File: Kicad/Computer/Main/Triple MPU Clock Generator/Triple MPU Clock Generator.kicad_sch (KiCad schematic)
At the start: 48 parts, among them CN1 CA0612KRX7R9BB100, CN2 CA0612KRX7R9BB100, CN3 CA0612KRX7R9BB100, CN4 CA0612KRX7R9BB100, CN5 CA0612KRX7R9BB100, CN7 CA0612KRX7R9BB100, CN8 CA0612KRX7R9BB100, IC1 AP7365-33WG-7, IC10 74LVC74APW,118, IC11 74LVC157APW,118, IC12 74LVC1G08GV,125, IC13 74LVC14APW,118, IC2 74LVC74APW,118, IC3 74LVC74APW,118, IC4 74LVC74APW,118, IC5 74LVC74APW,118, IC6 74LVC74APW,118, IC7 74LVC157APW,118, IC8 DS1813R-10+T&R, J10 Pin_Header_01x32, J11 Pin_Header_01x32, J2 Conn_02x32_Counter_Clockwise, J4 Conn_01x04_Socket, J5 Conn_01x04_Socket

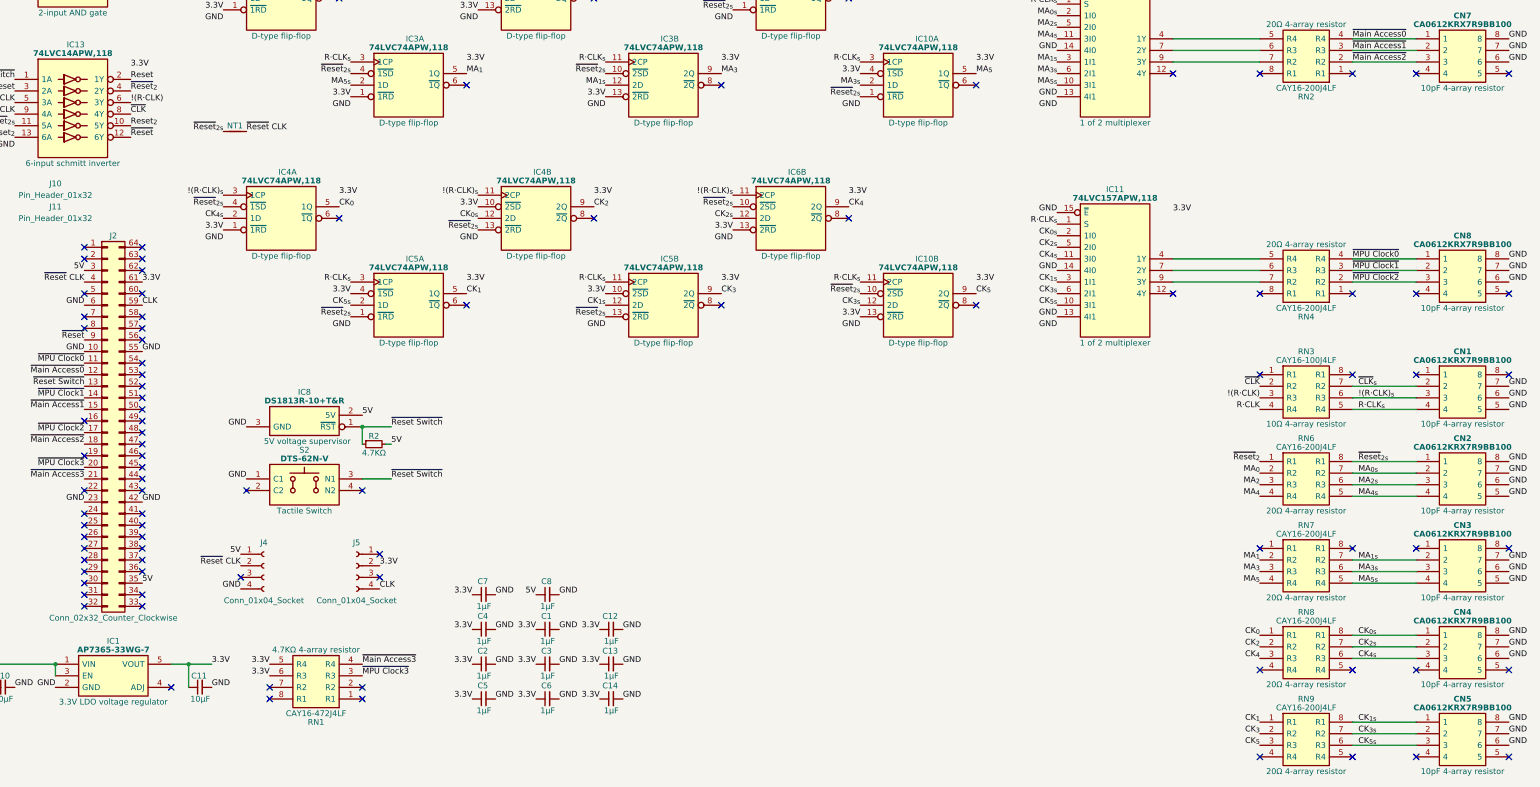
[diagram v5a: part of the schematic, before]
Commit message: Added a (potentially) 50MHz board.
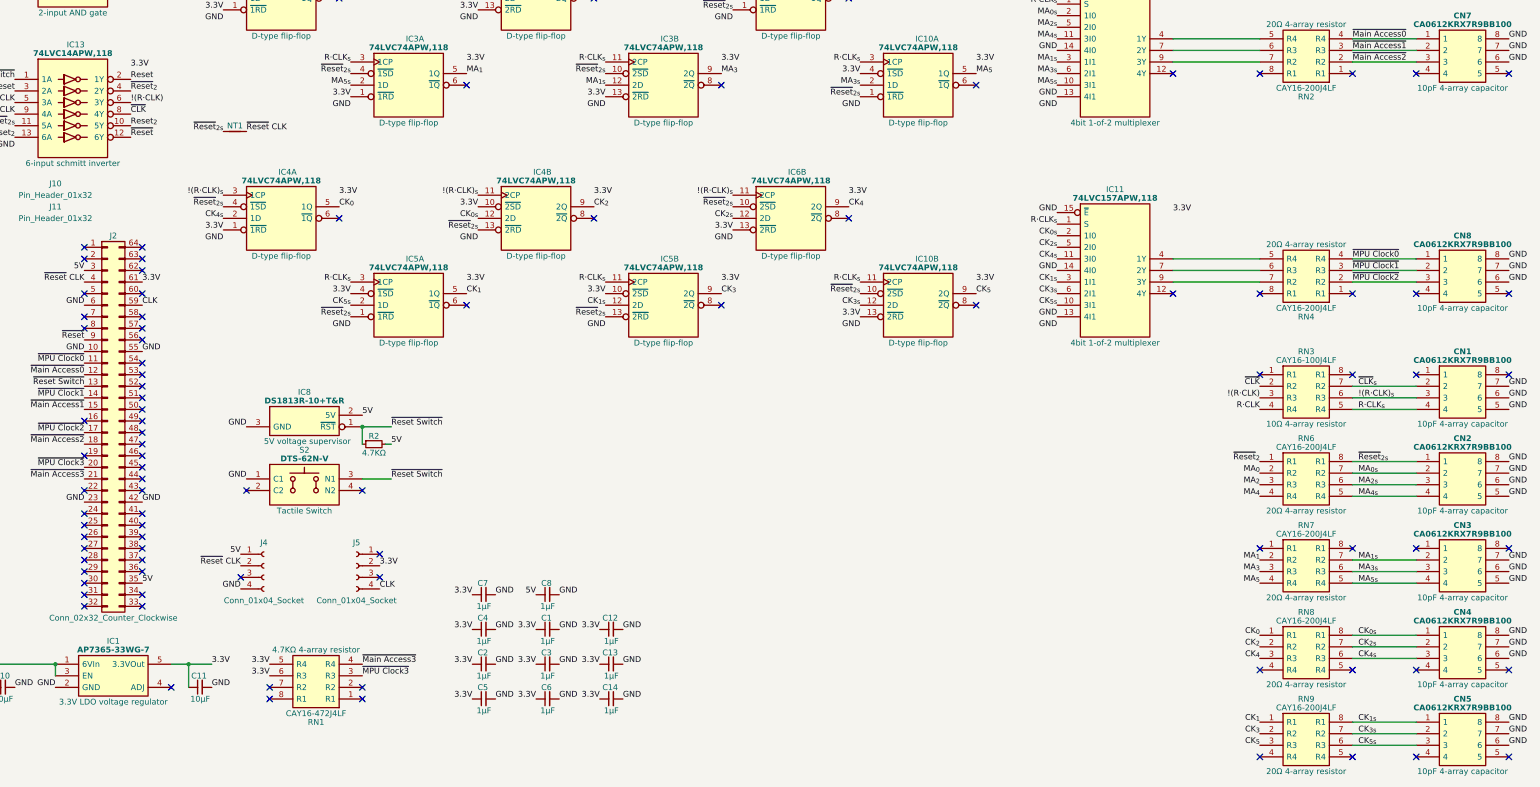
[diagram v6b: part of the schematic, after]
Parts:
- IC1: footprint SOT95P285X130-5N -> SamacSys_Parts:SOT95P285X130-5N; Garbage (none) -> DiodesZetex AP7365-33WG-7, LDO Voltage Regulator, 600mA, 3.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
- IC10, IC2, IC3, IC4, IC5, IC6: footprint SOP65P640X110-14N -> SamacSys_Parts:SOP65P640X110-14N; Garbage (none) -> 74LVC74A - Dual D-type flip-flop with set and reset; positi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
- IC11, IC7: footprint SOP65P640X110-16N -> SamacSys_Parts:SOP65P640X110-16N; Garbage (none) -> NEXPERIA - 74LVC157APW,118 - MUX, QUAD, 8 I/P, TSSOP-16
- IC12: footprint SOT95P275X110-5N -> SamacSys_Parts:SOT95P275X110-5N; Garbage (none) -> NEXPERIA - 74LVC1G08GV,125 - LOGIC, AND GATE, DUAL I/P, SC-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
- IC13: footprint SOP65P640X110-14N -> SamacSys_Parts:SOP65P640X110-14N; Garbage (none) -> 74LVC14A - Hex inverting Schmitt trigger with 5 V tolerant 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
- IC8: footprint SOT95P237X112-3N -> SamacSys_Parts:SOT95P237X112-3N; Garbage (none) -> Maxim DS1813R-10+T&R, Voltage Supervisor 4.25 4.49 V, Reset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
- J4, J5: footprint Connector_PinSocket_2.54mm:PinSocket_1x04_P2.54mm_Vertical -> (none)
- NT1: footprint NetTie:NetTie-2_SMD_Pad0.5mm -> SamacSys_Parts:NetTie:NetTie-2_SMD_Pad0.5mm
- RN1: Garbage (none) -> Bourns CAY16 Series 4.7k +/-5% Isolated SMT Resistor Array,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
- RN2, RN4, RN6, RN7, RN8, RN9: Arrow Part Number CAY16-331J4LF -> (none); Arrow Price/Stock https://www.arrow.com/en/products/cay16-331j4lf/bourns?regi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 -> (none)
- RN3: Garbage (none) -> Bourns CAY16 Series 10 +/-5% Isolated SMT Resistor Array, 4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
- S2: footprint DTS62NV -> SamacSys_Parts:DTS62NV; Garbage (none) -> Tactile Switches Through Hole 6*6

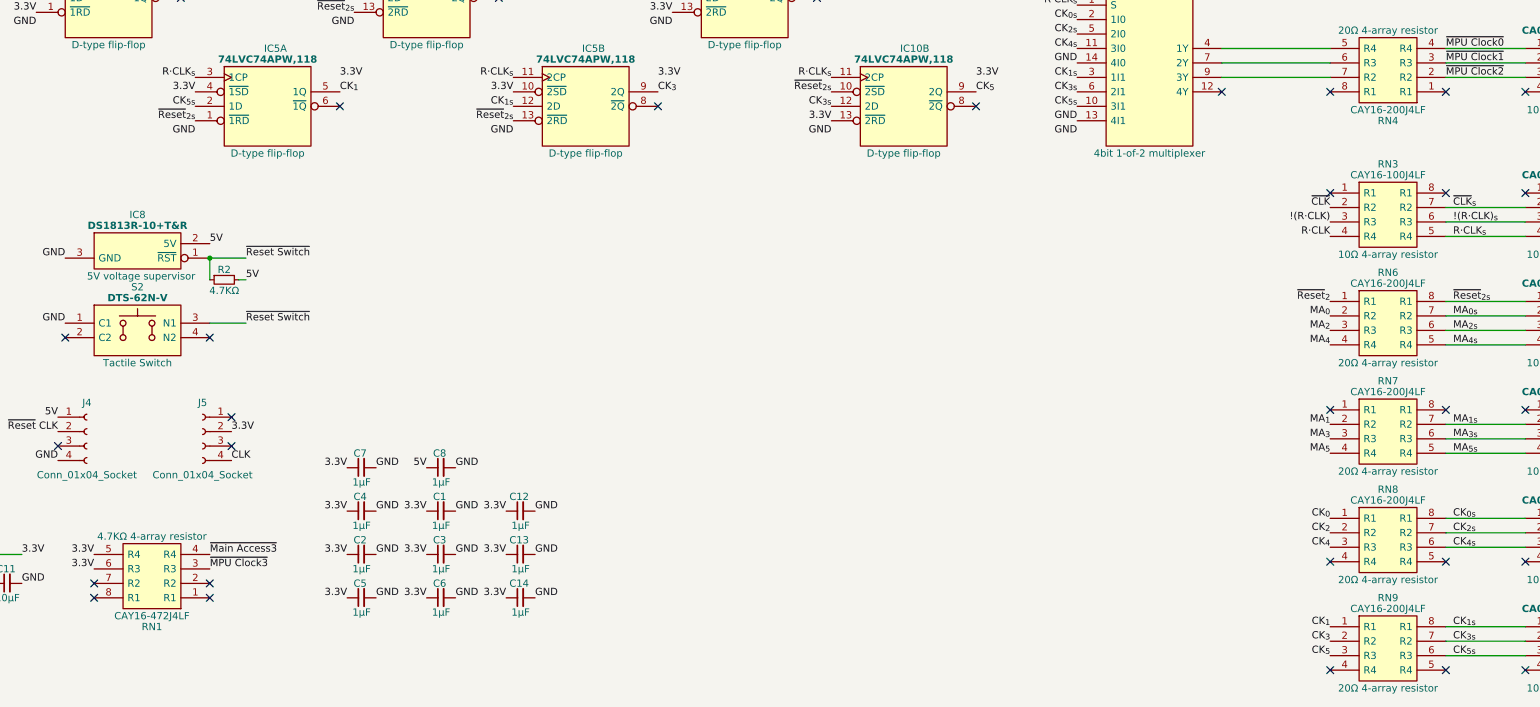
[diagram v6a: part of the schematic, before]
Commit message: Generated Gerbers for clock generators.
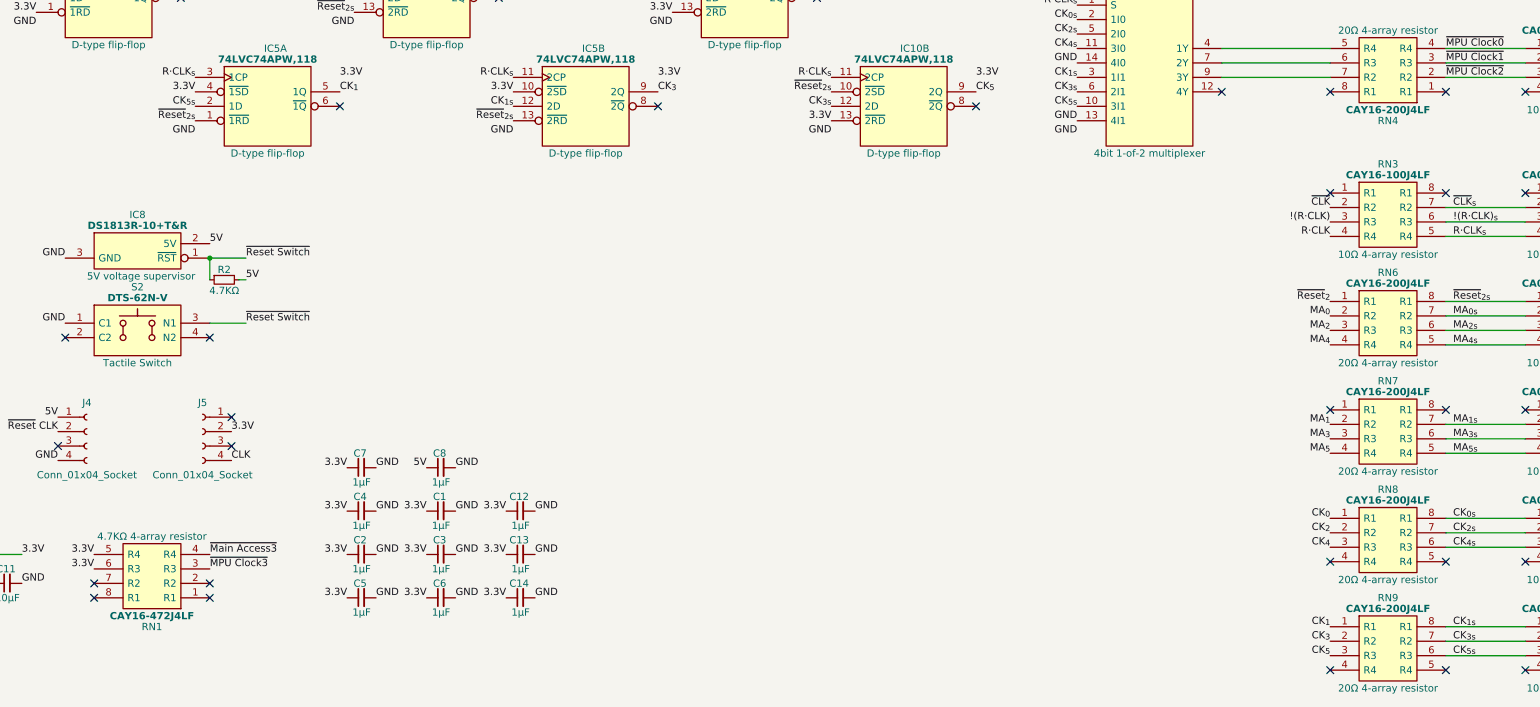
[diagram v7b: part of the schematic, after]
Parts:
- IC1: Garbage DiodesZetex AP7365-33WG-7, LDO Voltage Regulator, 600mA, 3.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 -> (none)
- IC8: Garbage Maxim DS1813R-10+T&R, Voltage Supervisor 4.25 4.49 V, Reset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 -> (none)
- J4, J5: footprint (none) -> Connector_PinSocket_2.54mm:PinSocket_1x04_P2.54mm_Vertical
- NT1: footprint SamacSys_Parts:NetTie:NetTie-2_SMD_Pad0.5mm -> NetTie:NetTie-2_SMD_Pad0.5mm
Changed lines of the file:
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@@
 			)
 		)
-		(property "Footprint" ""
+		(property "Footprint" "Connector_PinSocket_2.54mm:PinSocket_1x04_P2.54mm_Vertical"
 			(at 95.25 189.23 0)
 			(effects
@@
 				(font
 					(size 1.27 1.27)
+					(bold yes)
 				)
 			)
@@
 			)
 		)
-		(property "Footprint" "SamacSys_Parts:NetTie:NetTie-2_SMD_Pad0.5mm"
+		(property "Footprint" "NetTie:NetTie-2_SMD_Pad0.5mm"
 			(at 107.315 100.965 0)
 			(effects
@@
 				(font
 					(size 1.27 1.27)
+					(bold yes)
 				)
 			)
@@
 				(font
 					(size 1.27 1.27)
+					(bold yes)
 				)
 			)
@@
 			)
 		)
-		(property "Footprint" ""
+		(property "Footprint" "Connector_PinSocket_2.54mm:PinSocket_1x04_P2.54mm_Vertical"
 			(at 115.57 189.23 0)
 			(effects
@@
 				(font
 					(size 1.27 1.27)
+					(bold yes)
 				)
 			)
@@
 				(font
 					(size 1.27 1.27)
+					(bold yes)
 				)
 			)
@@
 			)
 		)
-		(property "Garbage" "DiodesZetex AP7365-33WG-7, LDO Voltage Regulator, 600mA, 3.3 V +/-2%, 2  6 Vin, 5-Pin SOT-25"
-			(at 71.12 248.412 0)
-			(effects
-				(font
-					(size 1.27 1.27)
-				)
-				(justify left)
-				(hide yes)
-			)
-		)
 		(pin "1"
 		)
@@
 			)
 		)
-		(property "Garbage" "Maxim DS1813R-10+T&R, Voltage Supervisor 4.25  4.49 V, Reset Input, 3-Pin SOT-23"
-			(at 91.44 158.75 0)
-			(effects
-				(font
-					(size 1.27 1.27)
-				)
-				(hide yes)
-			)
-		)
 		(pin "1"
 		)
@@
 				(font
 					(size 1.27 1.27)
+					(bold yes)
 				)
 			)
@@
 				(font
 					(size 1.27 1.27)
+					(bold yes)
 				)
 			)

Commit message: Rounded clock generator traces.
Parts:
- IC11, IC7: Garbage NEXPERIA - 74LVC157APW,118 - MUX, QUAD, 8 I/P, TSSOP-16 -> (none)
- IC12: Garbage NEXPERIA - 74LVC1G08GV,125 - LOGIC, AND GATE, DUAL I/P, SC-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 -> (none)
- RN1: Garbage Bourns CAY16 Series 4.7k +/-5% Isolated SMT Resistor Array,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 -> (none)
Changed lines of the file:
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@@
 		)
 		(property "Silkscreen" "74LVC157"
-			(at 281.94 142.24 0)
-			(effects
-				(font
-					(size 1.27 1.27)
-				)
-				(hide yes)
-			)
-		)
-		(property "Garbage" "NEXPERIA - 74LVC157APW,118 - MUX, QUAD, 8 I/P, TSSOP-16"
-			(at 269.24 111.76 0)
+			(at 293.37 150.495 0)
 			(effects
 				(font
 					(size 1.27 1.27)
 				)
+				(justify left)
 				(hide yes)
 			)
@@
 		)
 		(property "Silkscreen" "'1G08"
-			(at 53.34 70.485 0)
-			(effects
-				(font
-					(size 1.27 1.27)
-				)
-				(hide yes)
-			)
-		)
-		(property "Garbage" "NEXPERIA - 74LVC1G08GV,125 - LOGIC, AND GATE, DUAL I/P, SC-74A-5"
-			(at 40.64 59.69 0)
+			(at 64.77 76.835 0)
 			(effects
 				(font
 					(size 1.27 1.27)
 				)
+				(justify left)
 				(hide yes)
 			)
@@
 		)
 		(property "Silkscreen" "74LVC157"
-			(at 281.94 93.98 0)
-			(effects
-				(font
-					(size 1.27 1.27)
-				)
-				(hide yes)
-			)
-		)
-		(property "Garbage" "NEXPERIA - 74LVC157APW,118 - MUX, QUAD, 8 I/P, TSSOP-16"
-			(at 269.24 63.5 0)
+			(at 293.37 102.235 0)
 			(effects
 				(font
 					(size 1.27 1.27)
 				)
+				(justify left)
 				(hide yes)
 			)
@@
 			(effects
 				(font
-					(size 1.27 1.27)
-				)
-				(hide yes)
-			)
-		)
-		(property "Garbage" "Bourns CAY16 Series 4.7k +/-5% Isolated SMT Resistor Array, 4 Resistors, 0.25W total 1206 (3216M) package Convex"
-			(at 116.84 218.44 0)
-			(effects
-				(font
